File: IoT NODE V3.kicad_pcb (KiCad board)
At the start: 2 copper layers, 120 x 90 mm, 146 parts, among them J1 Screw_Terminal_01x16, J3 UPLOADER, J4 Screw_Terminal_01x12, SW1 RST, SW2 SW_DIP_x04, SW3 BOOT, SW4 FACTORY RST, U1 ESP32-WROOM-32U, U11 AMS1117-33, U12 PCF8574ATS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

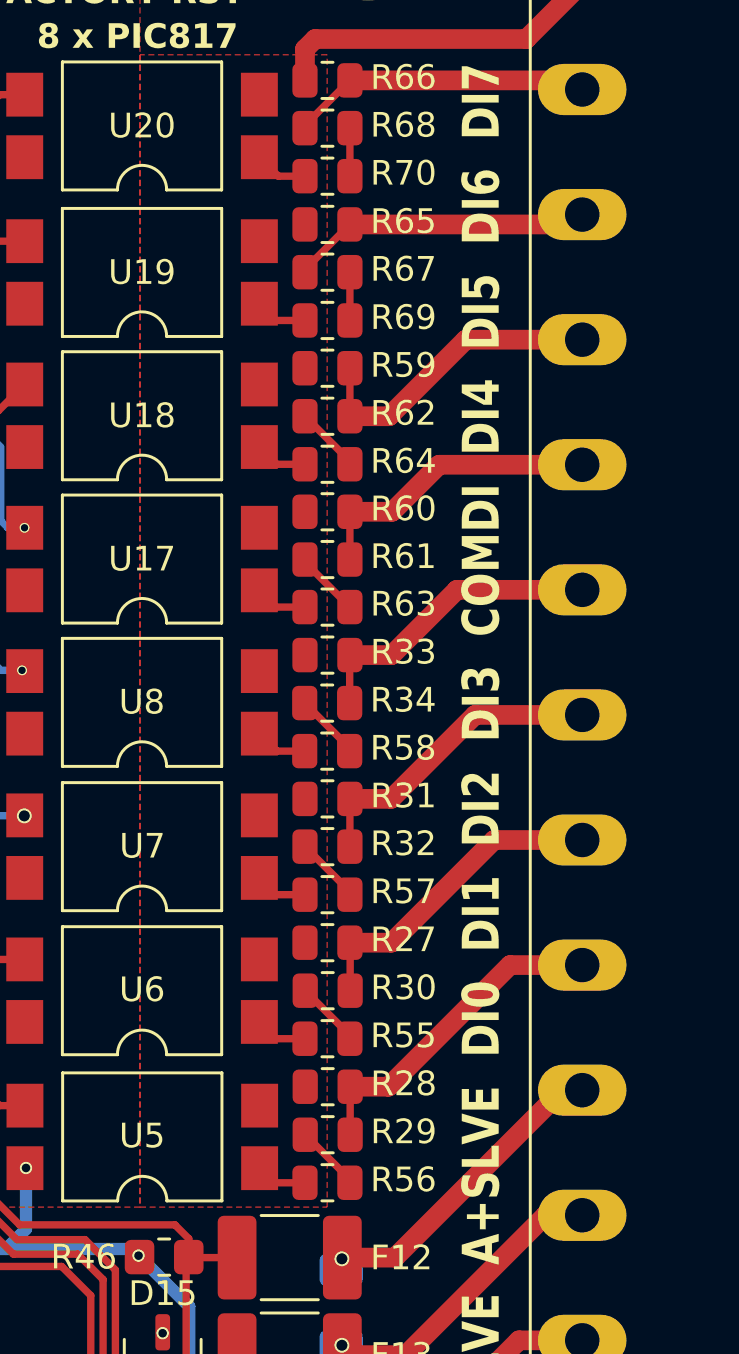
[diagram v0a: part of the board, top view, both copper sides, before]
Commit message: ganti resistor 4K3 DI
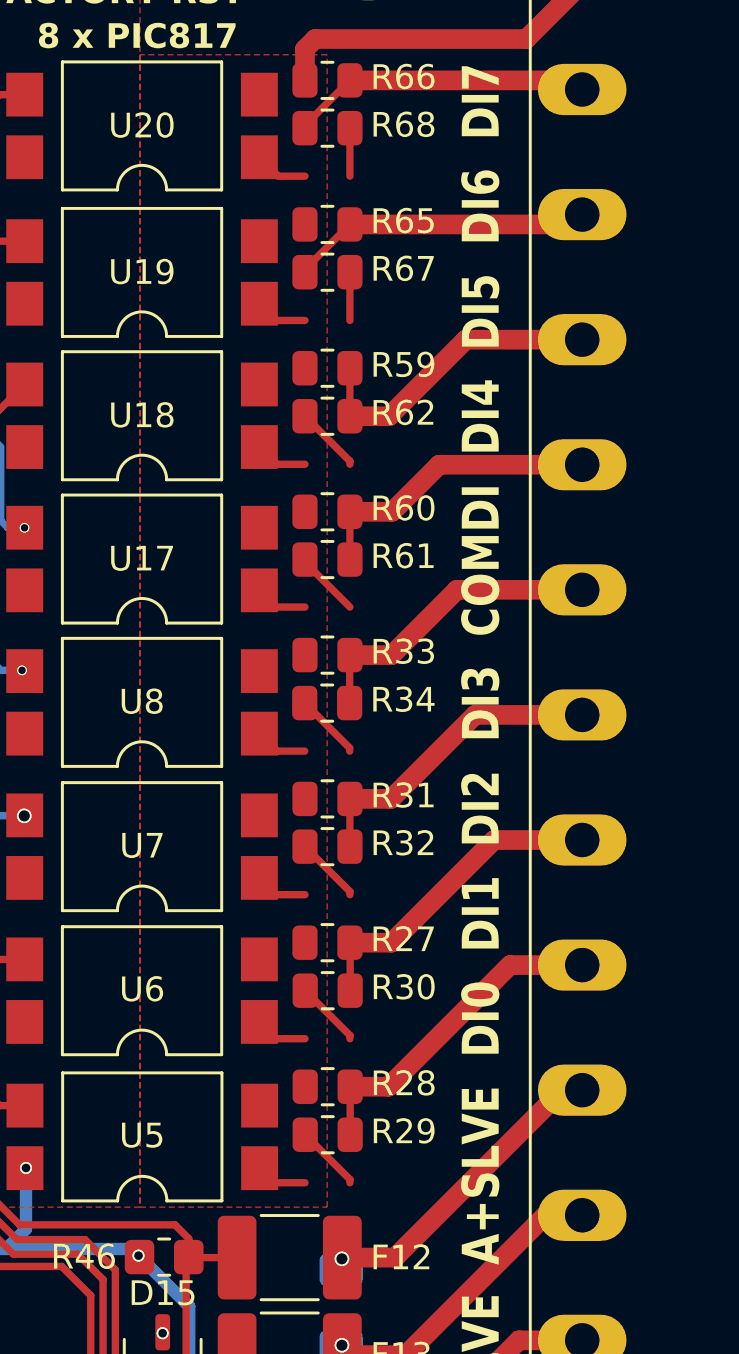
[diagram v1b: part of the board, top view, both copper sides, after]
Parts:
- removed R55, R56, R57, R58, R63, R64, R69, R70: 470, Resistor_SMD:R_0805_2012Metric
- R29, R30, R32, R34, R61, R62, R67, R68: value 470 -> 4k3
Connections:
- net GND renamed Earth_Protective
- U17 pad 1: Net-(R63-Pad2) -> Net-(R61-Pad2)
- U18 pad 1: Net-(R64-Pad2) -> Net-(R62-Pad2)
- U19 pad 1: Net-(R69-Pad2) -> Net-(R67-Pad2)
- U20 pad 1: Net-(R70-Pad2) -> Net-(R68-Pad2)
- U5 pad 1: Net-(R56-Pad2) -> Net-(R29-Pad2)
- U6 pad 1: Net-(R55-Pad2) -> Net-(R30-Pad2)
- U7 pad 1: Net-(R57-Pad2) -> Net-(R32-Pad2)
- U8 pad 1: Net-(R58-Pad2) -> Net-(R34-Pad2)
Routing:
- net Net-(R70-Pad2): track 2.17 -> 0.00 mm
- net Net-(R68-Pad2): track 1.95 -> 4.12 mm
- net Net-(R64-Pad2): track 2.14 -> 0.00 mm
- net Net-(R62-Pad2): track 2.71 -> 4.85 mm
- net Net-(R58-Pad2): track 2.14 -> 0.00 mm
- net Net-(R34-Pad2): track 2.71 -> 4.84 mm
- net Net-(R32-Pad2): track 2.71 -> 4.84 mm
- net Net-(R57-Pad2): track 2.13 -> 0.00 mm
- net Net-(R69-Pad2): track 2.13 -> 0.00 mm
- net Net-(R67-Pad2): track 1.96 -> 4.09 mm
- net Net-(R63-Pad2): track 2.13 -> 0.00 mm
- net Net-(R55-Pad2): track 2.13 -> 0.00 mm
- net Net-(R30-Pad2): track 2.70 -> 4.84 mm
- net Net-(R61-Pad2): track 2.69 -> 4.82 mm
- net Net-(R29-Pad2): track 2.70 -> 4.79 mm
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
